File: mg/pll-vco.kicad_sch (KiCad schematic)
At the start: 18 parts, among them U4 LMC555CTPX_NOPB, U5 SN74LVC2G74YZPR, U7 CD74HC4046APWR, Y2 ACOUSTIC TX

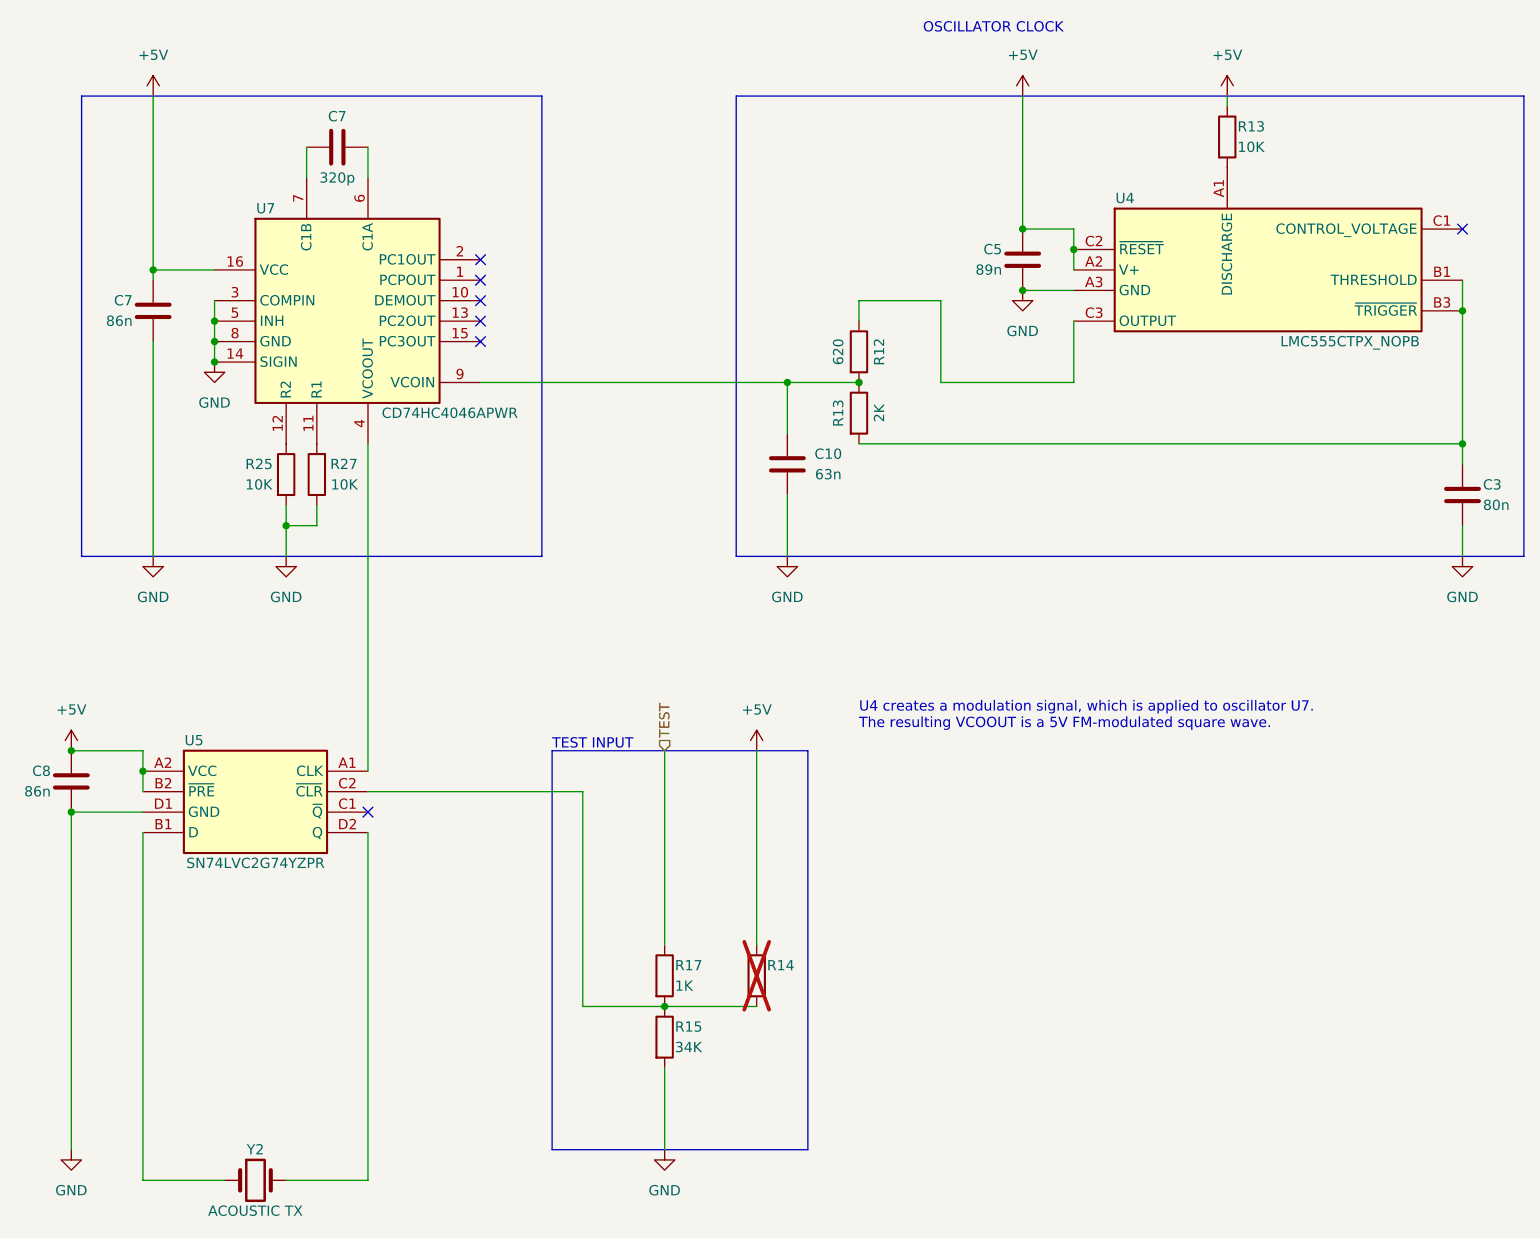
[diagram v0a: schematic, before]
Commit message: Fully reverse engineered. Added comments to schematic.
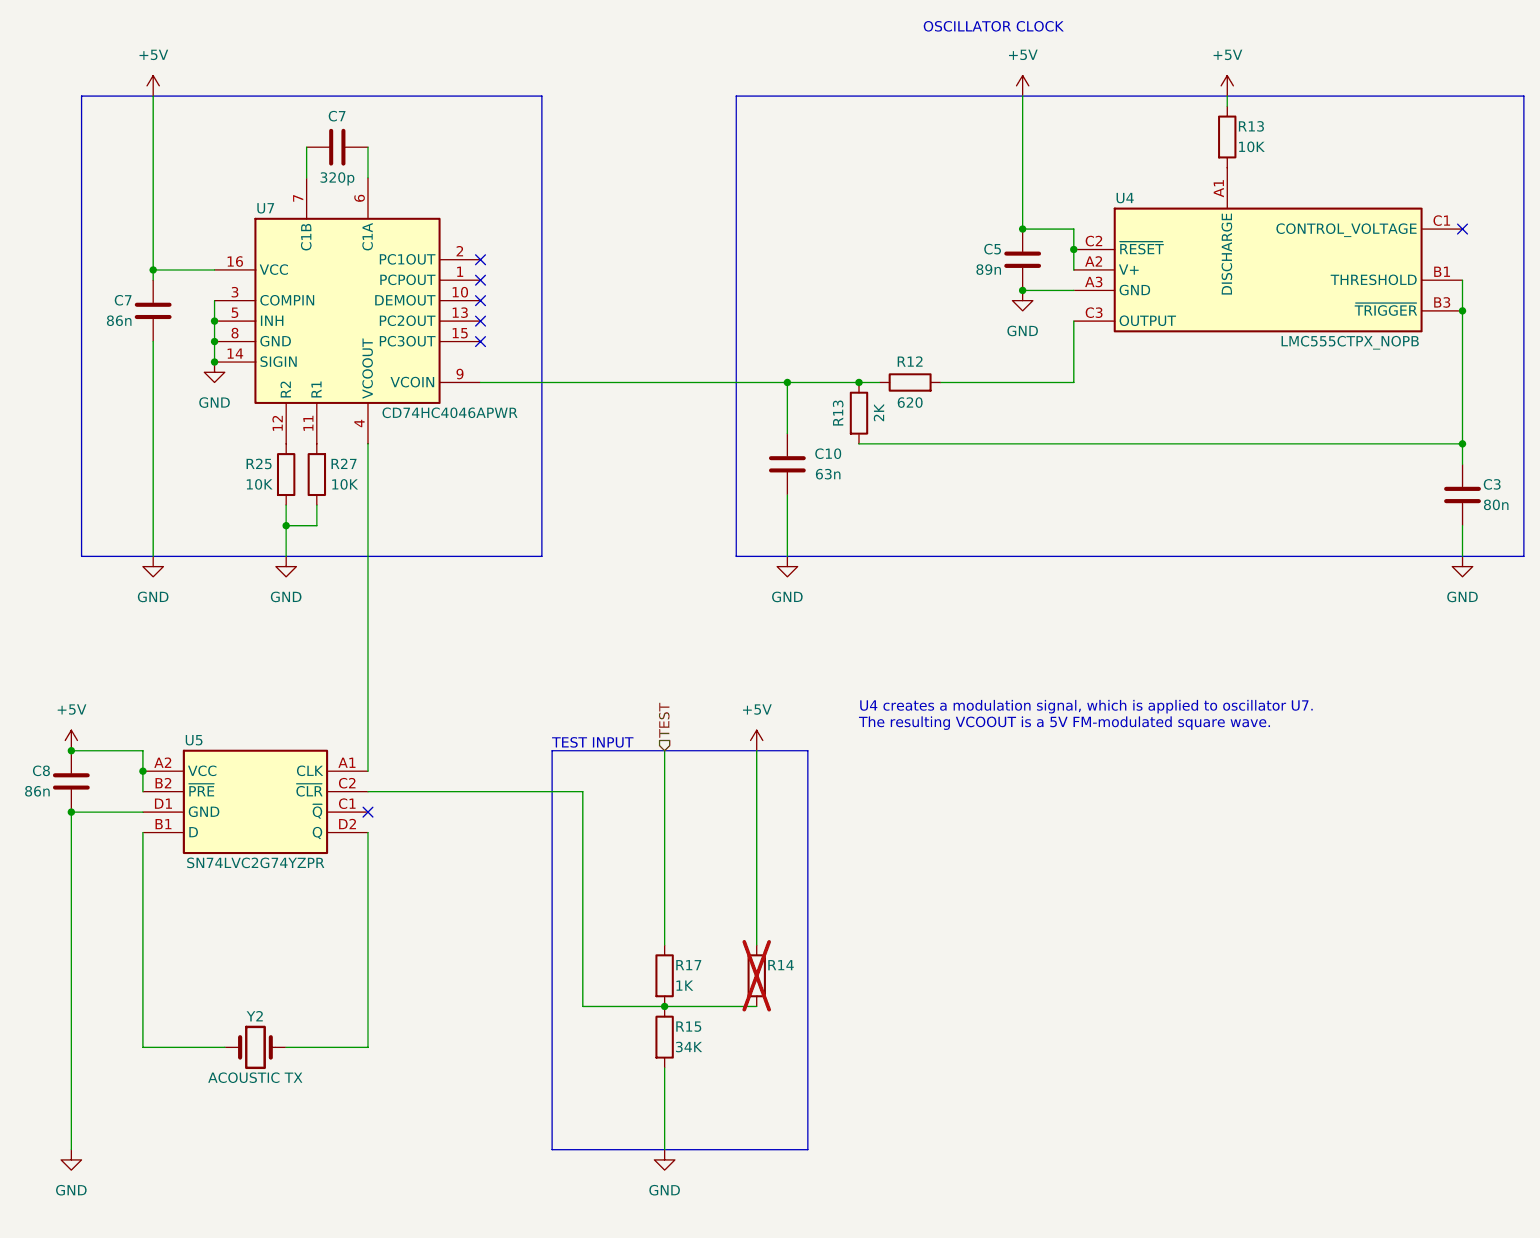
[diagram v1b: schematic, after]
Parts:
- R14: value (none) -> ~
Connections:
- net at C10.2, R13.1, U7.9 (VCOIN): now also R12.1; no longer R12.2
- net at U4.C3 (OUTPUT): now also R12.2; no longer R12.1
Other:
- moved on the sheet: R12, Y2
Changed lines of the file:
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@@
   (junction (at 85.09 72.39) (diameter 0) (color 0 0 0 0)
   )
+  (junction (at 85.09 69.85) (diameter 0) (color 0 0 0 0)
+  )
+  (junction (at 185.42 55.88) (diameter 0) (color 0 0 0 0)
+  )
+  (junction (at 156.21 74.93) (diameter 0) (color 0 0 0 0)
+  )
+  (junction (at 76.2 123.19) (diameter 0) (color 0 0 0 0)
+  )
+  (junction (at 85.09 67.31) (diameter 0) (color 0 0 0 0)
+  )
+  (junction (at 67.31 128.27) (diameter 0) (color 0 0 0 0)
+  )
+  (junction (at 93.98 92.71) (diameter 0) (color 0 0 0 0)
+  )
   (junction (at 165.1 74.93) (diameter 0) (color 0 0 0 0)
-  )
-  (junction (at 85.09 69.85) (diameter 0) (color 0 0 0 0)
-  )
-  (junction (at 185.42 55.88) (diameter 0) (color 0 0 0 0)
-  )
-  (junction (at 156.21 74.93) (diameter 0) (color 0 0 0 0)
-  )
-  (junction (at 76.2 123.19) (diameter 0) (color 0 0 0 0)
-  )
-  (junction (at 85.09 67.31) (diameter 0) (color 0 0 0 0)
-  )
-  (junction (at 67.31 128.27) (diameter 0) (color 0 0 0 0)
-  )
-  (junction (at 93.98 92.71) (diameter 0) (color 0 0 0 0)
   )
   (no_connect (at 118.11 59.69))
@@
     (stroke (width 0) (type default))
   )
-  (wire (pts (xy 76.2 130.81) (xy 76.2 173.99))
+  (wire (pts (xy 76.2 130.81) (xy 76.2 157.48))
     (stroke (width 0) (type default))
   )
@@
     (stroke (width 0) (type default))
   )
-  (wire (pts (xy 104.14 173.99) (xy 93.98 173.99))
+  (wire (pts (xy 104.14 157.48) (xy 93.98 157.48))
     (stroke (width 0) (type default))
   )
@@
     (stroke (width 0) (type default))
   )
-  (wire (pts (xy 165.1 64.77) (xy 175.26 64.77))
-    (stroke (width 0) (type default))
-  )
   (wire (pts (xy 140.97 152.4) (xy 152.4 152.4))
     (stroke (width 0) (type default))
   )
-  (wire (pts (xy 165.1 67.31) (xy 165.1 64.77))
-    (stroke (width 0) (type default))
-  )
   (wire (pts (xy 191.77 58.42) (xy 191.77 60.96))
     (stroke (width 0) (type default))
@@
     (stroke (width 0) (type default))
   )
+  (wire (pts (xy 165.1 74.93) (xy 167.64 74.93))
+    (stroke (width 0) (type default))
+  )
   (wire (pts (xy 240.03 96.52) (xy 240.03 92.71))
     (stroke (width 0) (type default))
   )
-  (wire (pts (xy 175.26 64.77) (xy 175.26 74.93))
-    (stroke (width 0) (type default))
-  )
   (wire (pts (xy 191.77 67.31) (xy 191.77 74.93))
     (stroke (width 0) (type default))
@@
     (stroke (width 0) (type default))
   )
-  (wire (pts (xy 104.14 130.81) (xy 104.14 173.99))
+  (wire (pts (xy 104.14 130.81) (xy 104.14 157.48))
     (stroke (width 0) (type default))
   )
@@
     (stroke (width 0) (type default))
   )
-  (wire (pts (xy 76.2 173.99) (xy 86.36 173.99))
+  (wire (pts (xy 76.2 157.48) (xy 86.36 157.48))
     (stroke (width 0) (type default))
   )
@@
     )
   )
-  (symbol (lib_id "Device:Crystal") (at 90.17 173.99 0) (unit 1)
-    (in_bom yes) (on_board yes) (dnp no)
-    (property "Reference" "Y2" (at 90.17 170.18 0)
-      (effects (font (size 1.27 1.27)))
-    )
-    (property "Value" "ACOUSTIC TX" (at 90.17 177.8 0)
-      (effects (font (size 1.27 1.27)))
-    )
-    (property "Footprint" "mg_footprints:piezo" (at 90.17 173.99 0)
-      (effects (font (size 1.27 1.27)) hide)
-    )
-    (property "Datasheet" "~" (at 90.17 173.99 0)
+  (symbol (lib_id "Device:Crystal") (at 90.17 157.48 0) (unit 1)
+    (in_bom yes) (on_board yes) (dnp no)
+    (property "Reference" "Y2" (at 90.17 153.67 0)
+      (effects (font (size 1.27 1.27)))
+    )
+    (property "Value" "ACOUSTIC TX" (at 90.17 161.29 0)
+      (effects (font (size 1.27 1.27)))
+    )
+    (property "Footprint" "mg_footprints:piezo" (at 90.17 157.48 0)
+      (effects (font (size 1.27 1.27)) hide)
+    )
+    (property "Datasheet" "~" (at 90.17 157.48 0)
       (effects (font (size 1.27 1.27)) hide)
     )
@@
       (effects (font (size 1.27 1.27)) (justify left))
     )
-    (property "Value" "" (at 153.67 149.86 0)
+    (property "Value" "~" (at 153.67 149.86 0)
       (effects (font (size 1.27 1.27)) (justify left))
     )
@@
     )
   )
-  (symbol (lib_id "Device:R") (at 165.1 71.12 0) (unit 1)
-    (in_bom yes) (on_board yes) (dnp no)
-    (property "Reference" "R12" (at 167.64 71.12 90)
-      (effects (font (size 1.27 1.27)))
-    )
-    (property "Value" "620" (at 162.56 71.12 90)
-      (effects (font (size 1.27 1.27)))
-    )
-    (property "Footprint" "mg_footprints:C_0603Metric" (at 163.322 71.12 90)
-      (effects (font (size 1.27 1.27)) hide)
-    )
-    (property "Datasheet" "~" (at 165.1 71.12 0)
-      (effects (font (size 1.27 1.27)) hide)
-    )
+  (symbol (lib_id "Device:R") (at 171.45 74.93 90) (unit 1)
+    (in_bom yes) (on_board yes) (dnp no)
+    (property "Reference" "R12" (at 171.45 72.39 90)
+      (effects (font (size 1.27 1.27)))
+    )
+    (property "Value" "620" (at 171.45 77.47 90)
+      (effects (font (size 1.27 1.27)))
+    )
+    (property "Footprint" "mg_footprints:C_0603Metric" (at 171.45 76.708 90)
+      (effects (font (size 1.27 1.27)) hide)
+    )
+    (property "Datasheet" "~" (at 171.45 74.93 0)
+      (effects (font (size 1.27 1.27)) hide)
+    )
